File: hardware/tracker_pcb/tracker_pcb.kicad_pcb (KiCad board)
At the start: 4 copper layers, 119 x 57 mm, 49 parts, among them IC1 DRV8244HQRYJRQ1, IC2 DRV8244HQRYJRQ1, IC3 THVD1426DRLR, J1 256-406, J3 Screw_Terminal_01x03, Q1 LTV-817S-TA1, U2 ESP32C6_SEEED, U3 TPS62933FDRLR, X1 256-402

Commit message: WIP it so good
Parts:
- removed J3: Screw_Terminal_01x03, Connector_PinHeader_2.54mm:PinHeader_1x03_P2.54mm_Vertical
- added C11: 100nF, Capacitor_SMD:C_0603_1608Metric, F.Cu at (136.7, 113.8)
- added D4: 1N4148W(SOD-123), Diode_SMD:D_0603_1608Metric, F.Cu at (168.9, 104.4)
- added D6: 1N4148W(SOD-123), Diode_SMD:D_0603_1608Metric, F.Cu at (176.6, 104.4)
- added J2: JL308-25409G01, TerminalBlock_TE-Connectivity:TerminalBlock_TE_282834-9_1x09_P2.54mm_Horizontal, F.Cu at (159.8, 110.3)
- added LED1: LED/RED/0603, LED_SMD:LED_0603_1608Metric, F.Cu at (167.3, 104.4)
- added LED3: LED/RED/0603, LED_SMD:LED_0603_1608Metric, F.Cu at (175.0, 104.4)
- added Q2: LTV-817S-TA1, footprint:LTV-817S_LTO, F.Cu at (168.7, 96.7)
- added Q3: LTV-817S-TA1, footprint:LTV-817S_LTO, F.Cu at (176.4, 96.7)
- added R12: 3.9k, Resistor_SMD:R_0603_1608Metric, F.Cu at (170.5, 104.4)
- added R13: 47k, Resistor_SMD:R_0603_1608Metric, F.Cu at (166.6, 89.8)
- added R14: 3.9k, Resistor_SMD:R_0603_1608Metric, F.Cu at (178.2, 104.4)
- added R15: 47k, Resistor_SMD:R_0603_1608Metric, F.Cu at (174.3, 89.8)
- moved R9 16.1 mm to (159.0, 89.8)
- moved Q1 13.8 mm to (161.1, 96.7), turned to 90 degrees
- moved R11 12.1 mm to (162.9, 104.4), turned to 90 degrees
- moved D5 11.5 mm to (161.3, 104.4), turned to 90 degrees
- moved LED2 11.3 mm to (159.7, 104.4), turned to -90 degrees
- moved C9 1.67 mm to (157.5, 86.3), turned to 90 degrees
- moved C10 0.40 mm to (114.4, 99.1)
- moved C8 0.38 mm to (108.5, 99.1)
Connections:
- net /IN0 renamed /DIG0
- R9 pad 1: /Isolated Input/VDD -> VDD
- U2 pad 2: unconnected-(U2-D1-Pad2) -> /DIG1
- U2 pad 3: unconnected-(U2-D2-Pad3) -> /DIG2
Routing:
- net /VRPP: track 0.00 -> 84.6 mm
- net /motor4: track 5.36 -> 34.4 mm, vias 1 -> 2
- net /motor0: track 27.0 -> 48.5 mm, vias 2 -> 3
- net /motor1: track 20.8 -> 38.8 mm, vias 1 -> 2
- net /motor2: track 20.9 -> 36.6 mm, vias 1 -> 2
- net VDD: track 18.6 -> 34.3 mm, vias 44 -> 46
- net /motor3: track 5.27 -> 19.3 mm, vias 1 -> 2
- net /DIG0: track 0.00 -> 9.34 mm
- net /DIG1: track 0.00 -> 8.67 mm
- net /DIG2: track 0.00 -> 8.67 mm
- net GND: track 10.8 -> 16.3 mm
- net /Isolated Input1/IN+: track 0.00 -> 5.32 mm
- net /Isolated Input2/IN+: track 0.00 -> 5.32 mm
- net Net-(D6-K): track 0.00 -> 3.88 mm
- net Net-(D4-K): track 0.00 -> 3.88 mm
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- added copper zone on B.Cu, net GND

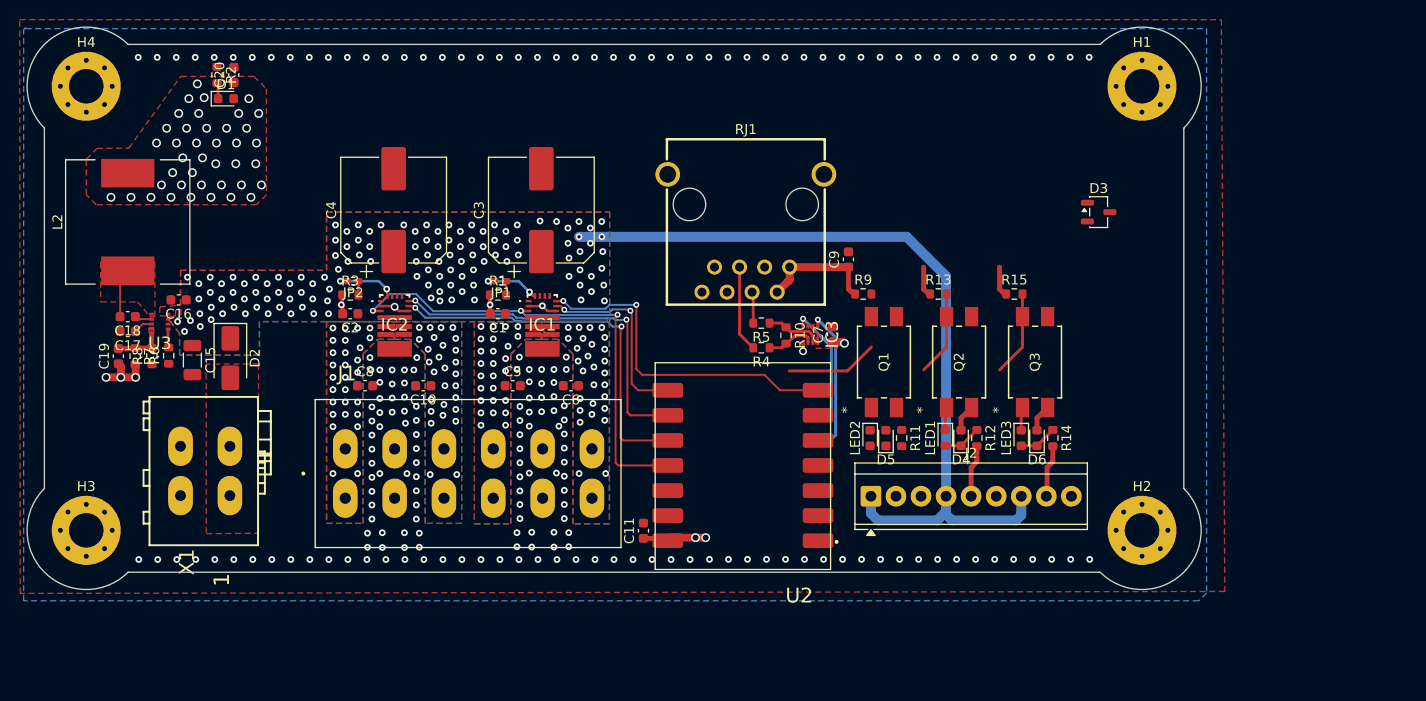
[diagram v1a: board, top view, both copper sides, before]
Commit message: Complete but optos are using 5v pullups instead of 3v3.  No bueno
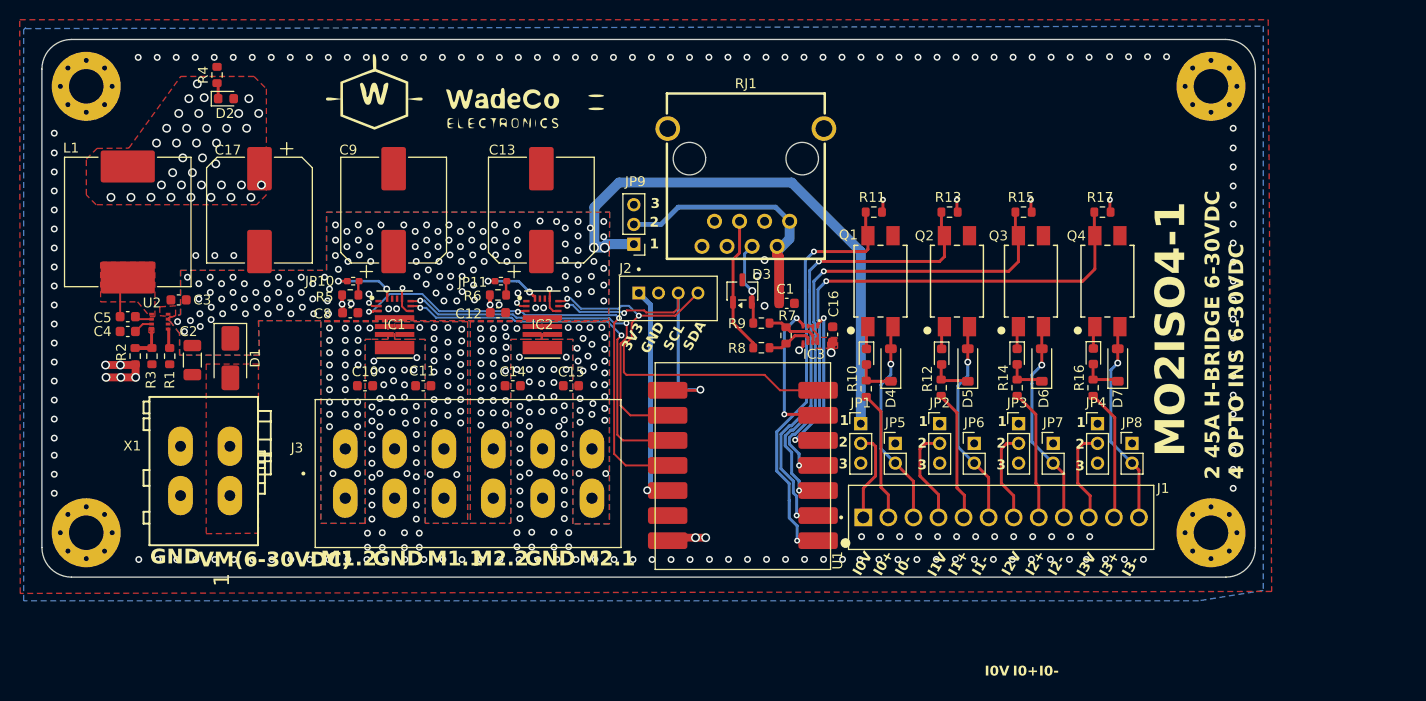
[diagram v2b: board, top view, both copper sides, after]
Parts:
- removed the C11 at (136.7, 113.8)
- removed C19: 47pF, Capacitor_SMD:C_0603_1608Metric
- removed C20: 10uF, Capacitor_SMD:C_0603_1608Metric
- removed the R6 at (88.6, 96.0)
- added C17: 100uF, Capacitor_SMD:CP_Elec_10x10.5, F.Cu at (97.8, 81.3)
- added D7: 1N4148W(SOD-123), Diode_SMD:D_SOD-123, F.Cu at (184.8, 97.0)
- added J1: JL308-25412G01, footprint:TE_1-282834-2, F.Cu at (173.0, 112.4)
- added JP1: Jumper_3_Open, Connector_PinHeader_2.00mm:PinHeader_1x03_P2.00mm_Vertical, F.Cu at (158.8, 102.9)
- added JP2: Jumper_3_Open, Connector_PinHeader_2.00mm:PinHeader_1x03_P2.00mm_Vertical, F.Cu at (166.8, 102.9)
- added JP3: Jumper_3_Open, Connector_PinHeader_2.00mm:PinHeader_1x03_P2.00mm_Vertical, F.Cu at (174.8, 102.9)
- added JP4: Jumper_3_Open, Connector_PinHeader_2.00mm:PinHeader_1x03_P2.00mm_Vertical, F.Cu at (182.8, 102.9)
- added JP5: Jumper_2_Open, Connector_PinHeader_2.00mm:PinHeader_1x02_P2.00mm_Vertical, F.Cu at (162.2, 104.9)
- added JP6: Jumper_2_Open, Connector_PinHeader_2.00mm:PinHeader_1x02_P2.00mm_Vertical, F.Cu at (170.2, 104.9)
- added JP7: Jumper_2_Open, Connector_PinHeader_2.00mm:PinHeader_1x02_P2.00mm_Vertical, F.Cu at (178.2, 104.9)
- added JP8: Jumper_2_Open, Connector_PinHeader_2.00mm:PinHeader_1x02_P2.00mm_Vertical, F.Cu at (186.2, 104.9)
- added JP9: Jumper_3_Open, Connector_PinHeader_2.00mm:PinHeader_1x03_P2.00mm_Vertical, F.Cu at (135.8, 84.8)
- added LED4: C72039, LED_SMD:LED_0603_1608Metric, F.Cu at (182.3, 96.1)
- added Q4: LTV-817S-TA1-D, footprint:LTV-817S_LTO, F.Cu at (183.8, 88.5)
- added R1: 61.9k, Resistor_SMD:R_0603_1608Metric, F.Cu at (88.7, 96.1)
- added R16: 1k, Resistor_SMD:R_0603_1608Metric, F.Cu at (182.3, 99.3)
- added R17: 27k, Resistor_SMD:R_0603_1608Metric, F.Cu at (183.2, 81.5)
- D4: renamed from D5; footprint Diode_SMD:D_0603_1608Metric -> Diode_SMD:D_SOD-123
- D5: renamed from D4; footprint Diode_SMD:D_0603_1608Metric -> Diode_SMD:D_SOD-123
- D6: footprint Diode_SMD:D_0603_1608Metric -> Diode_SMD:D_SOD-123
- IC1: renamed from IC2; footprint footprint:DRV8244HQRYJRQ1 -> footprint:RXZ0016A-MFG
- IC2: renamed from IC1; footprint footprint:DRV8244HQRYJRQ1 -> footprint:RXZ0016A-MFG
- J2: value JL308-25409G01 -> B4B-PH-K-S; footprint TerminalBlock_TE-Connectivity:TerminalBlock_TE_282834-9_1x09_P2.54mm_Horizontal -> footprint:JST_B4B-PH-K-S
- L1: renamed from L2; value 4.7uH -> 10uH; footprint Inductor_SMD:L_12x12mm_H6mm -> Inductor_SMD:L_Changjiang_FXL1350
- LED1: renamed from LED2; value LED/RED/0603 -> C72039
- LED2: renamed from LED1; value LED/RED/0603 -> C72039
- LED3: value LED/RED/0603 -> C72039
- Q1, Q2, Q3: value LTV-817S-TA1 -> LTV-817S-TA1-D
- R10: renamed from R11; value 3.9k -> 1k
- R11: renamed from R9; value 47k -> 27k
- R12, R14: value 3.9k -> 1k
- R13, R15: value 47k -> 27k
- R9: renamed from R5; value R_US -> 10
- moved D3 37.0 mm to (146.8, 89.5), turned to 90 degrees
- moved J2 28.7 mm to (139.2, 90.2), turned to 180 degrees
- moved R13 8.38 mm to (167.8, 81.5), turned to 180 degrees
- moved R11 8.37 mm to (160.1, 81.5), turned to 180 degrees
- moved R15 8.35 mm to (175.2, 81.5), turned to 180 degrees
- moved LED3 8.27 mm to (174.6, 96.1)
- moved LED2 8.25 mm to (166.9, 96.2)
- moved LED1 8.25 mm to (159.3, 96.2)
- moved Q3 8.21 mm to (176.0, 88.5)
- moved Q1 8.21 mm to (160.8, 88.5)
- moved Q2 8.20 mm to (168.5, 88.5)
- moved C1 7.67 mm to (151.2, 90.8), turned to 0 degrees
- moved D5 7.43 mm to (169.6, 97.0)
- moved D4 7.42 mm to (161.8, 97.0)
- moved D6 7.42 mm to (177.1, 97.0)
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- renumbered C9 to C1, C8 to C10, C10 to C11, C1 to C12, C3 to C13, C5 to C14, C6 to C15, C7 to C16, C15 to C2, C16 to C3, C17 to C4, C18 to C5, C2 to C8, C4 to C9, D2 to D1, D1 to D2, J1 to J3, JP2 to JP10, JP1 to JP11, R7 to R2, R8 to R3, R2 to R4, R3 to R5, R1 to R6, R10 to R7, R4 to R8, U2 to U1, U3 to U2
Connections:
- net /DIG0 renamed /Isolated Input/ISO_GPIO
- net /DIG1 renamed /Isolated Input1/ISO_GPIO
- net /DIG2 renamed /Isolated Input2/ISO_GPIO
- C1 pad 1: VDD -> Net-(JP9-C)
- C12 pad 1: /VRPP -> VRPP
- C13 pad 1: /VRPP -> VRPP
- C2 pad 1: /VRPP -> VRPP
- C3 pad 1: /VRPP -> VRPP
- C8 pad 1: /VRPP -> VRPP
- C9 pad 1: /VRPP -> VRPP
- D1 pad 1: /VRPP -> VRPP
- D4 pad 2: GND -> /Isolated Input/IN-
- D5 pad 2: GND -> /Isolated Input1/IN-
- D6 pad 2: GND -> /Isolated Input2/IN-
- IC1 pad 13: unconnected-(IC2-DIAG-Pad13) -> GND
- IC1 pad 4: /VRPP -> VRPP
- IC2 pad 13: unconnected-(IC1-DIAG-Pad13) -> GND
- IC2 pad 4: /VRPP -> VRPP
- J2 pad 1: /VRPP -> V3V3
- J2 pad 2: /Isolated Input/IN+ -> GND
- J2 pad 3: GND -> /motor3
- J2 pad 4: /VRPP -> /motor4
- Q1 pad 2: GND -> /Isolated Input/IN-
- Q2 pad 2: GND -> /Isolated Input1/IN-
- Q3 pad 2: GND -> /Isolated Input2/IN-
- RJ1 pad 1: VDD -> Net-(JP9-C)
- RJ1 pad 2: VDD -> Net-(JP9-C)
- U1 pad 12: unconnected-(U2-VCC_3V3-Pad12) -> V3V3
- U1 pad 4: unconnected-(U2-D3-Pad4) -> /Isolated Input3/ISO_GPIO
- U2 pad 3: /VRPP -> VRPP
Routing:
- net VRPP: track 0.00 -> 84.7 mm, vias 0 -> 132
- net /VRPP: track 84.6 -> 0.00 mm, vias 125 -> 0
- net /Isolated Input3/ISO_GPIO: track 0.00 -> 56.3 mm, vias 0 -> 2
- net /Isolated Input2/ISO_GPIO: track 8.67 -> 51.9 mm, vias 0 -> 2
- net /Isolated Input1/ISO_GPIO: track 8.67 -> 48.0 mm, vias 0 -> 2
- net /Isolated Input/ISO_GPIO: track 9.34 -> 43.4 mm, vias 0 -> 2
- net Net-(JP9-C): track 0.00 -> 26.1 mm
- net V3V3: track 0.00 -> 23.1 mm, vias 0 -> 1
- net /Isolated Input/IN-: track 0.00 -> 21.2 mm, vias 0 -> 1
- net /Isolated Input2/IN-: track 0.00 -> 21.2 mm, vias 0 -> 1
- net /Isolated Input1/IN-: track 0.00 -> 21.1 mm, vias 0 -> 1
- net /Isolated Input3/IN-: track 0.00 -> 20.9 mm, vias 0 -> 1
- net VDD: track 34.3 -> 20.3 mm, vias 46 -> 48
- net /Isolated Input3/IN+: track 0.00 -> 13.3 mm
- net /Isolated Input/IN+: track 0.00 -> 13.2 mm
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- added copper zone on B.Cu, net VRPP
- added copper zone on F.Cu, net VRPP
- added copper zone on In2.Cu, net VRPP
- removed copper zone on B.Cu, net /VRPP
- removed copper zone on F.Cu, net /VRPP
- removed copper zone on In2.Cu, net /VRPP
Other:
- board size 119 x 57 mm -> 123 x 54.5 mm
- board text added: "1"
- board text added: "2"
- board text added: "2 45A H-BRIDGE 6-30VDC 4 OPTO INS 6-30VDC"
- board text added: "3"
- board text added: "3V3"
- board text added: "GND"
- board text added: "I0+"
- board text added: "I0-"
- board text added: "I0V"
- board text added: "I1+"
- board text added: "I1-"
- board text added: "I1V"
- board text added: "I2+"
- board text added: "I2-"
- board text added: "I2V"
- board text added: "I3+"
- board text added: "I3-"
- board text added: "I3V"
- board text added: "M1.1"
- board text added: "M1.2"
- board text added: "M2.1"
- board text added: "M2.2"
- board text added: "MO2ISO4-1"
- board text added: "SCL"
- board text added: "SDA"
- board text added: "VM(6-30VDC)"

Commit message: WIP
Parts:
- removed D1: SS54, Diode_SMD:D_SMA
- removed JP10, JP11: SolderJumper_2_Open, Resistor_SMD:R_0402_1005Metric_Pad0.72x0.64mm_HandSolder
- added D8: SBR2U30P1-7, Diode_SMD:D_PowerDI-123, F.Cu at (143.4, 95.1)
- added JP12: Jumper_2_Open, Connector_PinHeader_2.00mm:PinHeader_1x02_P2.00mm_Vertical, F.Cu at (103.9, 90.9)
- added JP13: Jumper_2_Open, Connector_PinHeader_2.00mm:PinHeader_1x02_P2.00mm_Vertical, F.Cu at (118.9, 88.6)
- added U4: STPS30L30DJF-TR, footprint:SON_0L30DJF-TR_STM, F.Cu at (95.1, 94.2)
- R10, R12, R14, R16: footprint Resistor_SMD:R_0603_1608Metric -> Resistor_SMD:R_0805_2012Metric_Pad1.20x1.40mm_HandSolder
- moved R12 0.30 mm to (166.9, 99.6)
- moved R14 0.30 mm to (174.6, 99.6)
- moved R16 0.30 mm to (182.3, 99.6)
- moved R10 0.20 mm to (159.3, 99.6)
- moved C2 0.14 mm to (90.9, 96.6)
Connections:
- R11 pad 1: VDD -> V3V3
- R13 pad 1: VDD -> V3V3
- R15 pad 1: VDD -> V3V3
- R17 pad 1: VDD -> V3V3
- U1 pad 14: VDD -> Net-(U1-VUSB)
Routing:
- net V3V3: track 23.1 -> 86.3 mm, vias 1 -> 2
- net Net-(U1-VUSB): track 0.00 -> 28.2 mm, vias 0 -> 2
- net VDD: track 20.3 -> 13.3 mm, vias 48 -> 44
- net Net-(JP13-B): track 1.43 -> 4.85 mm
- net Net-(IC2-MODE): track 6.07 -> 7.49 mm
- net VRPP: vias 132 -> 124
- net GND: vias 268 -> 269

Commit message: Including LORA wio-sx1262
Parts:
- removed the C16 at (155.9, 93.9)
- removed D3: ESDA5V3L, Package_TO_SOT_SMD:SOT-23-3
- removed D8: SBR2U30P1-7, Diode_SMD:D_PowerDI-123
- removed JP12, JP13: Jumper_2_Open, Connector_PinHeader_2.00mm:PinHeader_1x02_P2.00mm_Vertical
- removed the R5 at (107.0, 89.9)
- removed the R6 at (122.0, 89.9)
- removed RJ1: RJ45 Shielded, footprint:RJ45-TH_R-RJ45S08P-B000
- added C18: 100nF, Capacitor_SMD:C_0603_1608Metric, F.Cu at (158.6, 104.2)
- added C19: 1uF, Capacitor_SMD:C_0603_1608Metric, F.Cu at (152.5, 96.8)
- added C20: 15pF, Capacitor_SMD:C_0603_1608Metric, F.Cu at (149.3, 96.7)
- added C21: 100nF, Capacitor_SMD:C_0603_1608Metric, F.Cu at (150.0, 78.4)
- added C22: 100nF, Capacitor_SMD:C_0603_1608Metric, F.Cu at (140.6, 81.7)
- added C23: 100nF, Capacitor_SMD:C_0603_1608Metric, F.Cu at (140.6, 83.2)
- added C24: 100nF, Capacitor_SMD:C_0603_1608Metric, F.Cu at (153.2, 76.0)
- added C25: 100nF, Capacitor_SMD:C_0603_1608Metric, F.Cu at (153.3, 71.8)
- added C7: 10uF, Capacitor_SMD:C_1206_3216Metric, F.Cu at (165.0, 99.2)
- added C8: 10uF, Capacitor_SMD:C_1206_3216Metric, F.Cu at (160.8, 104.2)
- added C9: 100nF, Capacitor_SMD:C_0603_1608Metric, F.Cu at (155.6, 95.4)
- added D1: ESDA5V3L, Package_TO_SOT_SMD:SOT-23-3, F.Cu at (159.8, 108.7)
- added IC4: WIO-SX1262, footprint:114993390, F.Cu at (161.9, 72.3)
- added J4: USB_C_Receptacle_USB2.0_16P, Connector_USB:USB_C_Receptacle_HRO_TYPE-C-31-M-12, F.Cu at (143.2, 114.6)
- added J5: B4B-XH-A, footprint:JST_B4B-XH-A, F.Cu at (158.7, 113.5)
- added JP10: Jumper_3_Open, Connector_PinHeader_2.00mm:PinHeader_1x03_P2.00mm_Vertical, F.Cu at (150.3, 72.8)
- added R10: 10, Resistor_SMD:R_0603_1608Metric, F.Cu at (156.2, 107.8)
- added R11: 10, Resistor_SMD:R_0603_1608Metric, F.Cu at (156.2, 109.5)
- added R2: 16.9k, Resistor_SMD:R_0603_1608Metric, F.Cu at (93.2, 71.0)
- added R20: 5.1k, Resistor_SMD:R_0603_1608Metric, F.Cu at (140.7, 107.2)
- added R21: 5.1k, Resistor_SMD:R_0603_1608Metric, F.Cu at (145.8, 107.2)
- added R22: 22R, Resistor_SMD:R_0603_1608Metric, F.Cu at (141.8, 102.1)
- added R23: 22R, Resistor_SMD:R_0603_1608Metric, F.Cu at (144.6, 102.1)
- added R24: 10k, Resistor_SMD:R_0603_1608Metric, F.Cu at (152.5, 98.5)
- added R25: 10k, Resistor_SMD:R_0603_1608Metric, F.Cu at (149.3, 98.5)
- added R26: 5.1k, Resistor_SMD:R_0603_1608Metric, F.Cu at (140.6, 86.2)
- added R3: 5.00k, Resistor_SMD:R_0603_1608Metric, F.Cu at (93.2, 72.8)
- added SW1: SKRKAEE020, footprint:SKRKAEE020, F.Cu at (150.5, 106.8)
- added SW2: SKRKAEE020, footprint:SKRKAEE020, F.Cu at (150.5, 102.0)
- added U4: TPS2117DRLR, footprint:SOTFL50P160X60-8N, F.Cu at (98.0, 71.8)
- added U5: TLV1117LV33DCYR, footprint:VREG_TLV1117LV33DCYR, F.Cu at (160.2, 97.2)
- added U6: ESP32-C6-MINI-1U-N4, footprint:XCVR_ESP32-C6-MINI-1U-N4, F.Cu at (148.4, 86.5)
- added U7: SN74LVC1G139, footprint:BGA8C50P2X4_89X189X50, F.Cu at (137.2, 86.0)
- IC1, IC2: value DRV8244HQRYJRQ1 -> DRV8244SQRYJRQ1; footprint footprint:RXZ0016A-MFG -> footprint:DRV8244HQRYJRQ1
- J2: value B4B-PH-K-S -> B6B-PH-K-S; footprint footprint:JST_B4B-PH-K-S -> footprint:JST_B6B-PH-K-S
- R7: value 120R -> 780R
- R8: value 10 -> 780R
- R9: value 10 -> 120R
- U1: value ESP32C6_SEEED -> USBLC6-2SC6; footprint footprint:MODULE_113991054 -> Package_TO_SOT_SMD:SOT-23-6
- moved JP9 33.8 mm to (163.8, 103.8), turned to 0 degrees
- moved J2 20.5 mm to (141.2, 69.8), turned to 0 degrees
- moved R7 17.5 mm to (140.6, 80.2), turned to 0 degrees
- moved R9 15.3 mm to (155.9, 106.2), turned to 0 degrees
- moved C1 14.1 mm to (137.3, 88.4), turned to 180 degrees
- moved R8 13.4 mm to (140.6, 84.7), turned to 0 degrees
- moved IC3 10.3 mm to (155.9, 104.0), turned to 0 degrees
- moved H1 9.52 mm to (203.8, 68.2)
- moved H2 9.52 mm to (203.8, 113.4)
- moved D5 9.18 mm to (178.8, 97.8)
- moved D6 9.18 mm to (186.2, 97.8)
- moved J1 9.18 mm to (182.1, 113.2)
- moved JP1 9.18 mm to (167.9, 103.7)
- moved JP2 9.18 mm to (175.9, 103.7)
- moved JP3 9.18 mm to (183.9, 103.7)
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- renumbered C8 to C10, C9 to C11, C10 to C12, C11 to C13, C12 to C14, C13 to C15, C14 to C16, C15 to C17, C17 to C6, R10 to R12, R11 to R13, R12 to R14, R13 to R15, R14 to R16, R15 to R17, R16 to R18, R17 to R19, R2 to R4, R3 to R5, R4 to R6, U4 to U2, U2 to U3
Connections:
- C1 pad 1: Net-(JP9-C) -> V33
- C6 pad 1: VDD -> Net-(U4-VIN2)
- IC1 pad 11: /motor1 -> /M1PWMF
- IC1 pad 12: /motor2 -> /M1PWMR
- IC1 pad 13: GND -> /NSS_CS1
- IC1 pad 14: unconnected-(IC1-SR-Pad14) -> /IO21
- IC1 pad 15: unconnected-(IC1-ITRIP-Pad15) -> /IO22
- IC1 pad 16: Net-(IC1-MODE) -> /Motor Control DRV8244_1/SDO
- IC1 pad 2: GND -> /IOUT1
- IC1 pad 3: /motor0 -> VRPP
- IC2 pad 11: /motor3 -> /M2PWMF
- IC2 pad 12: /motor4 -> /M2PWMR
- IC2 pad 13: GND -> /NSS_CS1
- IC2 pad 14: unconnected-(IC2-SR-Pad14) -> /IO21
- IC2 pad 15: unconnected-(IC2-ITRIP-Pad15) -> /Motor Control DRV8244_1/SDO
- IC2 pad 16: Net-(IC2-MODE) -> /IO23
- IC2 pad 2: GND -> /IOUT2
- IC2 pad 3: /motor0 -> VRPP
- IC3 pad 1: rs485_rx -> /RS485/rs485_rx
- IC3 pad 2: VDD -> V33
- IC3 pad 3: VDD -> V33
- IC3 pad 4: rs485_tx -> /RS485/rs485_tx
- IC3 pad 8: VDD -> V33
- J2 pad 1: V3V3 -> Net-(JP10-C)
- J2 pad 2: GND -> /IO21
- J2 pad 3: /motor3 -> /IO22
- J2 pad 4: /motor4 -> /IO23
- L1 pad 2: VDD -> Net-(U4-VIN2)
- R13 pad 1: V3V3 -> V33
- R15 pad 1: V3V3 -> V33
- R17 pad 1: V3V3 -> V33
- R19 pad 1: V3V3 -> V33
- R4 pad 2: VDD -> Net-(U4-VIN2)
- R7 pad 1: Net-(IC3-B) -> GND
- R7 pad 2: Net-(IC3-A) -> /IOUT1
- R8 pad 1: Net-(IC3-A) -> GND
- R8 pad 2: /RS485/A -> /IOUT2
- R9 pad 2: /RS485/B -> Net-(IC3-A)
- U1 pad 1: /Isolated Input/ISO_GPIO -> Net-(J4-D--PadA7)
- U1 pad 2: /Isolated Input1/ISO_GPIO -> GND
- U1 pad 3: /Isolated Input2/ISO_GPIO -> Net-(J4-D+-PadA6)
- U1 pad 4: /Isolated Input3/ISO_GPIO -> Net-(R23-Pad2)
- U1 pad 5: rs485_rx -> /VBUS
- U1 pad 6: rs485_tx -> Net-(R22-Pad2)
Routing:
- net V33: track 0.00 -> 119.2 mm, vias 0 -> 13
- net /VBUS: track 0.00 -> 102.3 mm, vias 0 -> 5
- net /IO22: track 0.00 -> 94.5 mm, vias 0 -> 7
- net /IO21: track 0.00 -> 91.0 mm, vias 0 -> 8
- net V3V3: track 86.3 -> 0.00 mm, vias 2 -> 0
- net /IO23: track 0.00 -> 78.5 mm, vias 0 -> 5
- net /SX_IRQ: track 0.00 -> 63.7 mm, vias 0 -> 2
- net /motor0: track 49.3 -> 0.00 mm, vias 3 -> 0
- net /IOUT1: track 0.00 -> 46.7 mm, vias 0 -> 2
- net /SX_BUSY: track 0.00 -> 46.0 mm, vias 0 -> 2
- net Net-(U4-VIN2): track 0.00 -> 43.4 mm
- net /motor4: track 43.0 -> 0.00 mm, vias 2 -> 0
- net VDD: track 13.3 -> 56.3 mm, vias 44 -> 5
- net /M1PWMF: track 0.00 -> 39.6 mm, vias 0 -> 4
- net /motor1: track 38.2 -> 0.00 mm, vias 2 -> 0
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- added copper zone on F.Cu, net /VBUS
- added copper zone on F.Cu, net Net-(U4-VIN2)
- added copper zone on F.Cu, net V33
- added copper zone on In2.Cu, net V33
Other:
- board size 123 x 54.5 mm -> 132.8 x 54.5 mm
- board text added: "CS3"
- board text added: "IO21"
- board text added: "IO22"
- board text added: "IO23"
- board text added: "NRST"
- board text removed: "SCL"
- board text removed: "SDA"

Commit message: update text
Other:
- board text added: "2 21A H-BRIDGE 6-30VDC 4 OPTO INS 6-30VDC"
- board text removed: "2 45A H-BRIDGE 6-30VDC 4 OPTO INS 6-30VDC"
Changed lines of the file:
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@@
 		)
 	)
-	(gr_text "2 45A H-BRIDGE 6-30VDC\n4 OPTO INS 6-30VDC"
+	(gr_text "2 21A H-BRIDGE 6-30VDC\n4 OPTO INS 6-30VDC"
 		(at 207.85 109.1 90)
 		(layer "F.SilkS")
@@
 		(polygon
 			(pts
-				(xy 158 68.3) (xy 158 68.3) (xy 158 67.3) (xy 148 67.3) (xy 148 82) (xy 158 82)
+				(xy 158 68.3) (xy 158 67.3) (xy 148 67.3) (xy 148 82) (xy 158 82)
 			)
 		)

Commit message: WIP
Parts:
- moved U5 0.55 mm to (160.2, 96.7)
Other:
- board text added: "0+"
- board text added: "0-"
- board text added: "0V"
- board text added: "1+"
- board text added: "1-"
- board text added: "1V"
- board text added: "2+"
- board text added: "2-"
- board text added: "2V"
- board text added: "3+"
- board text added: "3-"
- board text added: "3V"
- board text added: "IN1"
- board text added: "IN2"
- board text added: "IN3"
- board text added: "IN4"
- board text added: "POWER"
- board text removed: "I1+"
- board text removed: "I1-"
- board text removed: "I1V"
- board text removed: "I2+"
- board text removed: "I2-"
- board text removed: "I2V"
- board text removed: "I3+"
- board text removed: "I3-"
- board text removed: "I3V"

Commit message: VIA changes
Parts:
- R3: value 5.00k -> 5.1k
- R7, R8: value 780R -> 820R
- moved C16 0.12 mm to (123.6, 99.1)
- moved C17 0.12 mm to (129.5, 99.1)
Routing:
- net GND: vias 285 -> 288
- net /Motor Control DRV8244_1/OUT2: vias 27 -> 28
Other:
- board text added: "+V"
- board text added: "A"
- board text added: "B"
- board text removed: "3V3"
